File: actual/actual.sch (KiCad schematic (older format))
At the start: 32 parts

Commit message: Monday night hacking
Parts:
- removed C?: C, symbol Device:C
- removed P?: Conn_WallPlug_Earth, symbol Connector:Conn_WallPlug_Earth
- removed SW?: GROUND, symbol Switch:SW_SPDT
- added J?: IEC_SOCKET, symbol yga1:IEC_SOCKET
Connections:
- wire segments 80 -> 76
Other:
- moved on the sheet: F?, SW?
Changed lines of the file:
@@
 L Device:Fuse F?
 U 1 1 5C5654FC
-P 1600 5550
-F 0 "F?" V 1403 5550 50  0000 C CNN
-F 1 "Fuse" V 1494 5550 50  0000 C CNN
-F 2 "" V 1530 5550 50  0001 C CNN
-F 3 "~" H 1600 5550 50  0001 C CNN
-	1    1600 5550
+P 2150 5150
+F 0 "F?" V 1953 5150 50  0000 C CNN
+F 1 "Fuse" V 2044 5150 50  0000 C CNN
+F 2 "" V 2080 5150 50  0001 C CNN
+F 3 "~" H 2150 5150 50  0001 C CNN
+	1    2150 5150
 	0    1    1    0
 $EndComp
 $Comp
-L Connector:Conn_WallPlug_Earth P?
-U 1 1 5C5655DC
-P 1000 5350
-F 0 "P?" H 1065 5675 50  0000 C CNN
-F 1 "Conn_WallPlug_Earth" H 1065 5584 50  0000 C CNN
-F 2 "" H 1400 5350 50  0001 C CNN
-F 3 "~" H 1400 5350 50  0001 C CNN
-	1    1000 5350
-	1    0    0    -1
-$EndComp
-$Comp
 L power:Earth #PWR?
 U 1 1 5C56566E
-P 1300 5800
-F 0 "#PWR?" H 1300 5550 50  0001 C CNN
-F 1 "Earth" H 1300 5650 50  0001 C CNN
-F 2 "" H 1300 5800 50  0001 C CNN
-F 3 "~" H 1300 5800 50  0001 C CNN
-	1    1300 5800
-	1    0    0    -1
-$EndComp
-Wire Wire Line
-	1300 5650 1300 5800
-Wire Wire Line
-	1300 5450 1300 5550
-Wire Wire Line
-	1300 5550 1450 5550
-Wire Wire Line
-	2450 5550 1850 5550
-$Comp
-L Switch:SW_SPST SW?
-U 1 1 5C5657AA
-P 1500 5150
-F 0 "SW?" H 1500 5385 50  0000 C CNN
-F 1 "A.C." H 1500 5294 50  0000 C CNN
-F 2 "" H 1500 5150 50  0001 C CNN
-F 3 "" H 1500 5150 50  0001 C CNN
-	1    1500 5150
-	1    0    0    -1
-$EndComp
-Wire Wire Line
-	1300 5250 1300 5150
-Wire Wire Line
-	1700 5150 1850 5150
-$Comp
-L Switch:SW_SPDT SW?
-U 1 1 5C5658F5
-P 2050 5350
-F 0 "SW?" H 2050 5635 50  0000 C CNN
-F 1 "GROUND" H 2050 5544 50  0000 C CNN
-F 2 "" H 2050 5350 50  0001 C CNN
-F 3 "" H 2050 5350 50  0001 C CNN
-	1    2050 5350
-	-1   0    0    -1
-$EndComp
-Wire Wire Line
-	1850 5250 1850 5150
-Connection ~ 1850 5150
-Wire Wire Line
-	1850 5450 1850 5550
-Connection ~ 1850 5550
-Wire Wire Line
-	1850 5550 1750 5550
-$Comp
-L Device:C C?
-U 1 1 5C565A52
-P 2250 5750
-F 0 "C?" H 2365 5796 50  0000 L CNN
-F 1 "C" H 2365 5705 50  0000 L CNN
-F 2 "" H 2288 5600 50  0001 C CNN
-F 3 "~" H 2250 5750 50  0001 C CNN
-	1    2250 5750
-	1    0    0    -1
-$EndComp
-$Comp
-L power:Earth #PWR?
-U 1 1 5C565AE5
-P 2250 5950
-F 0 "#PWR?" H 2250 5700 50  0001 C CNN
-F 1 "Earth" H 2250 5800 50  0001 C CNN
-F 2 "" H 2250 5950 50  0001 C CNN
-F 3 "~" H 2250 5950 50  0001 C CNN
-	1    2250 5950
-	1    0    0    -1
-$EndComp
-Wire Wire Line
-	2250 5350 2250 5600
-Wire Wire Line
-	2250 5900 2250 5950
-Wire Wire Line
-	1850 5150 2450 5150
+P 1500 5800
+F 0 "#PWR?" H 1500 5550 50  0001 C CNN
+F 1 "Earth" H 1500 5650 50  0001 C CNN
+F 2 "" H 1500 5800 50  0001 C CNN
+F 3 "~" H 1500 5800 50  0001 C CNN
+	1    1500 5800
+	1    0    0    -1
+$EndComp
+Wire Wire Line
+	1400 5450 1400 5550
 $Comp
 L Device:Lamp LA?
@@
 Wire Wire Line
 	2550 2400 2550 2850
+Wire Wire Line
+	1400 5550 2450 5550
+Wire Wire Line
+	2000 5150 1950 5150
+Wire Wire Line
+	2300 5150 2450 5150
+$Comp
+L yga1:IEC_SOCKET J?
+U 1 1 5C64456C
+P 1400 5350
+F 0 "J?" H 950 5650 50  0000 C CNN
+F 1 "IEC_SOCKET" H 1100 5550 50  0000 C CNN
+F 2 "" H 1300 5350 50  0001 C CNN
+F 3 "" H 1300 5350 50  0001 C CNN
+	1    1400 5350
+	1    0    0    -1
+$EndComp
+Wire Wire Line
+	1400 5250 1400 5150
+$Comp
+L Switch:SW_SPST SW?
+U 1 1 5C5657AA
+P 1750 5150
+F 0 "SW?" H 1750 5385 50  0000 C CNN
+F 1 "A.C." H 1750 5294 50  0000 C CNN
+F 2 "" H 1750 5150 50  0001 C CNN
+F 3 "" H 1750 5150 50  0001 C CNN
+	1    1750 5150
+	1    0    0    -1
+$EndComp
+Wire Wire Line
+	1400 5150 1550 5150
+Wire Wire Line
+	1500 5350 1400 5350
+Wire Wire Line
+	1500 5350 1500 5800
 $EndSCHEMATC

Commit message: Update schematic and design reverb unit
Create a schematic to capture all the changes that have been done. There have been many small fiddle things but not even an electronic version of the full schematic.
Find a schematic for a reverb unit and add it to the amp schematic.
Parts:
- removed J?: CH2, symbol Connector:Conn_01x01_Male
- removed J?: CH1, symbol Connector:Conn_01x01_Male
- removed J?: CH1 volume pot (4M), symbol Connector:Conn_01x03_Male
- removed J?: Earth, symbol Connector:Conn_01x01_Male
- removed J?: CH2 volume pot (4M), symbol Connector:Conn_01x03_Male
- removed J?: Audio Out, symbol Connector:Conn_01x01_Male
- removed V? (x2): 12AX7A, symbol yga1:12AX7A
- added C1: 270uF 16V, symbol Device:CP
- added C10, C11, C15, C6: 0.1uF 400V, symbol Device:C
- added C12, C13: 8.2uF 250V, Capacitor_THT:CP_Radial_D8.0mm_P5.00mm, symbol Device:CP
- added C14: 0.047uF 600V, symbol Device:C
- added C16: 25uF 25V, symbol Device:C
- added C17: 0.02uF, 0.02uF, symbol Device:C
- added C18, C19: 0.01uF, symbol Device:C
- added C2, C4: 0.02uF 400V, symbol Device:C
- added C20: 47n, symbol Device:C
- added C27: 10uF 400V, symbol Device:C
- added C28: 1uF 16V, symbol Device:CP
- added C29, C33: 22uF 50V, symbol Device:CP
- added C3: 40uF, symbol Device:C
- added C30: 0.01uF 400V, symbol Device:C
- added C31: 100n, symbol Device:C
- added C32: 2n2, symbol Device:C
- added C34: 1uF, symbol Device:CP
- added C35: 220uF, symbol Device:CP
- added C36: 100nF 400V, symbol Device:C
- added C37: 10n, symbol Device:C
- added C38: 250pF, symbol Device:C
- added C5: 270pF, symbol Device:C
- added C7: 0.02uF, symbol Device:C
- added C8: 0.02 400V, symbol Device:C
- added C9: 0.1uF, symbol Device:C
- added D1: PH204, Diode_SMD:D_SMA, symbol Device:D
- added J1: in_lo, symbol yga1:AudioJack2_Switch
- added J10: effect return, symbol yga1:AudioJack2_Switch
- added J2: in_hi, symbol yga1:AudioJack2_Switch
- added J4: Tank IN, symbol Connector:Conn_Coaxial
- added J5: Audio Out, symbol Connector:AudioJack2
- added J6: Reverb Footswitch, symbol Connector:AudioJack2
- added J7: tremolo footswitch, symbol yga1:jack_0.25in_mono
- added J8: Tank OUT, symbol Connector:Conn_Coaxial
- added J9: effect send, symbol yga1:AudioJack2_Switch
- added R1, R19, R2: 68K, symbol Device:R
- added R10, R3, R37, R39, R56, R59: 1M, symbol Device:R
- added R11, R13, R15, R16, R25, R28, R40, R46, R49, R57: 100K, symbol Device:R
- added R12, R7: 820, symbol Device:R
- added R14: 10K 1W, symbol Device:R
- added R17: 27K, symbol Device:R
- added R18, R26, R27, R34, R51: 220K, symbol Device:R
- added R20, R22, R35, R36, R61: 470K, symbol Device:R
- added R21: 470, symbol Device:R
- added R23, R38: 4.7K, symbol Device:R
- added R24: 82K, symbol Device:R
- added R29, R30: 470 1W, symbol Device:R
- added R31: 150K, Resistor_THT:R_Axial_DIN0309_L9.0mm_D3.2mm_P12.70mm_Horizontal, symbol Device:R
- added R32: 15K, Resistor_THT:R_Axial_DIN0207_L6.3mm_D2.5mm_P10.16mm_Horizontal, symbol Device:R
- added R33: 56K, Resistor_THT:R_Axial_DIN0207_L6.3mm_D2.5mm_P10.16mm_Horizontal, symbol Device:R
- added R4: 4.7K 1W, symbol Device:R
- added R44: 10K 1/2W, symbol Device:R
- added R45: 1K, symbol Device:R
- added R47: 2.7K, symbol Device:R
- added R48: 100k, symbol Device:R
- added R5, R6: 2M2, symbol Device:R
- added R50: 1.5K, symbol Device:R
- added R52: 33K, symbol Device:R
- added R53: 2K2, symbol Device:R
- added R54: 4k7, symbol Device:R
- added R55: 1K 2W, symbol Device:R
- added R58: 1K5 1/2 watt, symbol Device:R
- added R8, R9: 100K 1/2W, symbol Device:R
- added RV1, RV2: 1M, symbol Device:R_POT
- added RV10: 100, symbol Device:R_POT
- added RV3: Treble Pot (250K), symbol Device:R_POT
- added RV4: Bass Pot (1M), symbol Device:R_POT
- added RV5: Intensity pot (1M), symbol Device:R_POT
- added RV6: Speed pot (250K), symbol Device:R_POT
- added RV7: 250kA, symbol Device:R_POT
- added RV8: 250kB, symbol Device:R_POT
- added RV9: 50kB, symbol Device:R_POT
- added S1: regular/crunch, symbol local:SW_SPDT
- added T2: 68348, symbol Device:Transformer_SP_1S
- added T3: Transformer_125ASE, symbol yga1:Transformer_125ASE
- added V1, V2, V3, V6, V8: 12AX7, Valve:Valve_ECC-83-1, symbol local:12AX7
- added V4, V5: 7027A, symbol yga1:7027A
- added V7: 12AT7, Valve:Valve_ECC-83-1, symbol local:12AT7
- added V9: EL84, symbol local:EL84
- R42: renamed from R?; value R -> 100K, 2W
- R43: renamed from R?; value 4.7K -> 4.7K 1W
- gave numbers to parts that had none: 20
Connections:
- net B+: now also R13.1, R14.2, R24.2, R25.1, R36.2, V2.1 (a), V6.6 (a)
- net Earth: now also C1.2, C12.1, C13.1, C14.2, C16.2, C27.2, C28.2, C29.2, C3.2, C33.2, C34.2, C35.2, C37.2, J1.S, J10.S, J2.S, J2.TN, J4.2 (Ext), J5.S, J6.S, J7.2, J8.2 (Ext), J9.S, R10.2, R12.2, R15.2, R17.2, R18.2, R23.2, R3.2, R33.2, R35.2, R38.2, R39.2, R40.2, R45.2, R46.2, R47.2, R50.2, R52.2, R55.2, R56.2, R58.2, R59.2, R6.2, R7.2, RV1.1, RV2.1, RV8.3, T2.4 (S1), T3.BLK (0h), V4.8 (C), V5.8 (C)
- net f1: now also V1.4 (f), V1.5 (f), V2.4 (f), V2.5 (f), V3.5 (f), V3.9 (f), V4.2, V5.7, V6.9 (f), V6.9 (f), V7.4 (f), V7.5 (f), V8.4 (f), V8.5 (f), V9.5 (f)
- net f2: now also V1.9 (f), V1.9 (f), V2.9 (f), V2.9 (f), V3.4 (f), V3.9 (f), V4.7, V5.2, V6.4 (f), V6.5 (f), V7.9 (f), V7.9 (f), V8.9 (f), V8.9 (f), V9.4 (f)
- net at D2.2 (A), T1.6: now also R31.2
- net V1: now reaches L1.1, SW3.2 (B)
- net V1: now also T2.2 (PM)
- net V2: now reaches C25.1, L1.2, R43.2
- net V2: now also R4.2, RV10.2
- new net: C28.1, R47.1, V1.3 (k)
- new net: C2.2, R8.1, V1.1 (a)
- new net: C27.1, R14.1, R8.2, R9.2
- new net: C2.1, RV1.3
- new net: C4.2, R9.1, V1.6 (a)
- new net: C4.1, RV2.3
- new net: R11.1, RV2.2
- new net: R11.2, V2.7 (g)
- new net: J1.TN, J2.T, R2.2
- new net: R1.1, R2.1, R3.1, S1.2, V1.2 (g)
- new net: J1.T, R1.2
- new net: R59.1, S1.1, V1.7 (g)
- new net: RV1.2, S1.3
- new net: C1.1, R7.1, V1.8 (k)
- new net: R13.2, V2.2 (g), V2.6 (a)
- new net: C34.1, R12.1, V2.8 (k)
- new net: C5.2, R15.1, R16.1, V2.3 (k)
- new net: C6.1, R16.2
- new net: C6.2, RV4.1
- new net: C5.1, RV3.1
- new net: C7.2, R17.1, RV4.3
- new net: C7.1, R18.1, RV3.3, RV4.2
- new net: J9.T, RV3.2
- new net: R53.1, V9.2 (g1)
- new net: C33.1, R55.1, V9.3 (k)
- new net: T3.BLU (IN-), V9.7 (a)
- new net: R54.2, V9.9 (g2)
- new net: C3.1, R4.1, R44.1, R49.1, R5.1, R54.1, R57.1, T3.BRN (IN+), V8.6 (a)
- new net: C20.1, R5.2, R6.1, V8.7 (g)
- new net: C31.2, R46.1, V8.8 (k)
- new net: C11.2, R25.2, V3.1 (a)
- new net: C9.1, R22.2, V3.2 (g)
- new net: R21.1, V3.3 (k), V3.8 (k)
- new net: R48.2, V7.6 (a)
- new net: C20.2, J10.T, R10.1, V7.7 (g)
- new net: C29.1, R45.1, V7.8 (k)
- new net: C32.2, R49.2, V7.1 (a)
- new net: RV8.2, V7.2 (g)
- new net: R50.1, V7.3 (k)
- new net: J10.TN, J9.TN
- new net: T2.1 (PR1), V4.3 (A)
- new net: R29.1, V4.4
- new net: C10.1, R27.1, V4.5 (G)
- new net: T2.3 (PR2), V5.3 (A)
- new net: R30.2, V5.4
- new net: C11.1, R26.2, V5.5 (G)
- new net: C8.1, R20.1, V3.7 (g)
- new net: C8.2, RV7.2
- new net: C9.2, R19.2, R23.1, R28.1
- new net: R19.1, R20.2, R21.2, R22.1
- new net: C10.2, R24.1, V3.6 (a)
- new net: C14.1, R26.1, R27.2, RV5.2
- new net: J5.T, R28.2, T2.5 (S2)
- new net: R29.2, RV10.1
- new net: R30.1, RV10.3
- new net: C15.1, R34.2
- new net: C15.2, RV5.1
- new net: R34.1, R35.1, V6.8 (k)
- new net: C17.2, R36.1, V6.1 (a), V6.7 (g)
- new net: C18.2, C19.1, J7.1, R37.1
- new net: C16.1, R37.2, R38.1, V6.3 (k)
- new net: C17.1, C18.1, RV6.1
- new net: C19.2, R39.1
- new net: R40.1, RV6.2
- new net: D1.1 (K), R31.1
- new net: C12.2, D1.2 (A), R32.2
- new net: C36.2, R57.2, V8.1 (a)
- new net: J6.T, J8.1 (In), R56.1, V8.2 (g)
- new net: C35.1, R58.1, V8.3 (k)
- new net: C30.2, R44.2, R48.1
- new net: C30.1, R61.2
- new net: R61.1, RV8.1
- new net: C32.1, R51.1
- new net: R51.2, R52.1, R53.2
- new net: J4.1 (In), T3.YEL (8h)
- new net: C31.1, RV7.3
- new net: C36.1, RV9.1
- new net: C37.1, RV9.3
- new net: C38.2, RV9.2
- new net: C38.1, RV7.1
- new net -40V: C13.2, R32.1, R33.1, RV5.3
- no-connect marks 0 -> 1
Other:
- moved on the sheet: C21, C22, C23, C24, C25, C26, D2, D3, D4, D5, D6, D7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

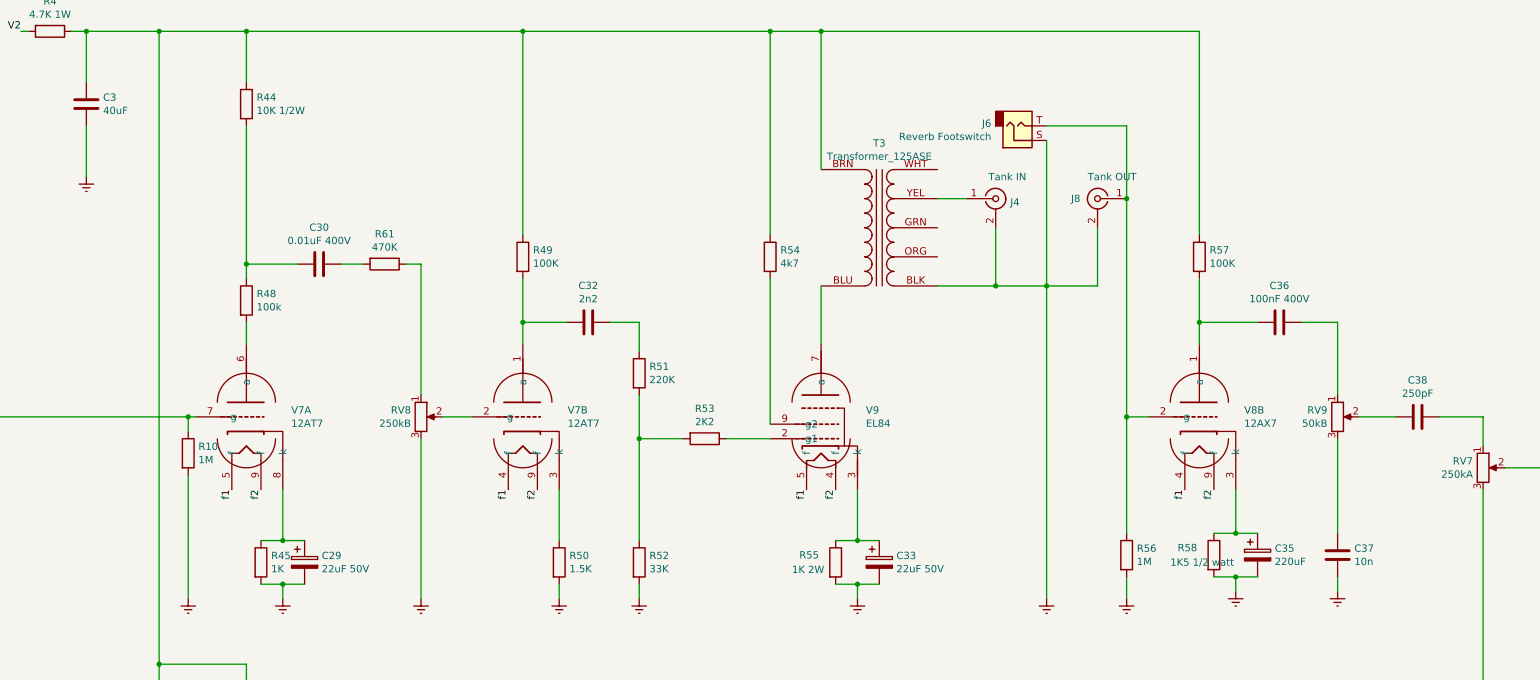
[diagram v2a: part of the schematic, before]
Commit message: parts list and order for reverb driver circuit
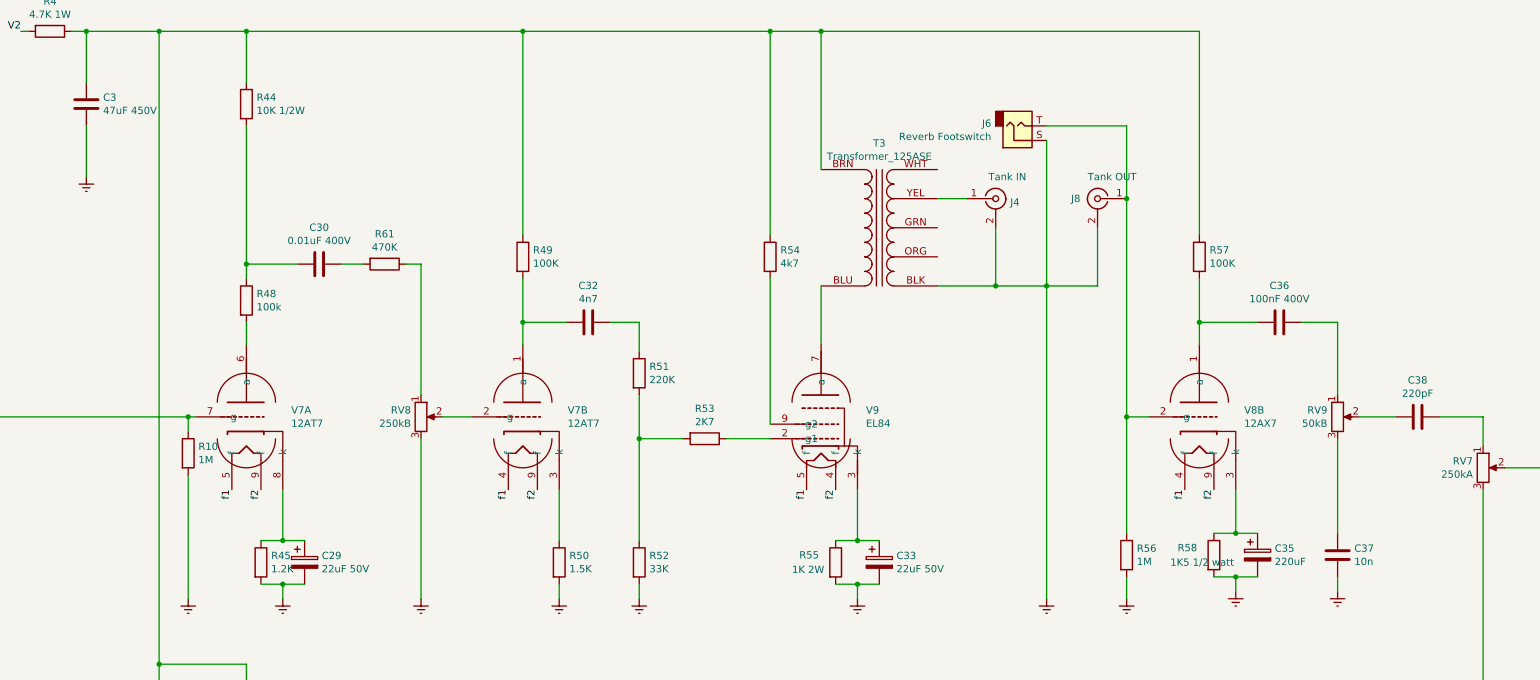
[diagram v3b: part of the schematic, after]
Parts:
- C3: value 40uF -> 47uF 450V
- C32: value 2n2 -> 4n7
- C38: value 250pF -> 220pF
- R45: value 1K -> 1.2K
- R53: value 2K2 -> 2K7
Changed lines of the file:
@@
 P 3350 9550
 F 0 "R45" H 3420 9596 50  0000 L CNN
-F 1 "1K" H 3420 9505 50  0000 L CNN
+F 1 "1.2K" H 3420 9505 50  0000 L CNN
 F 2 "" V 3280 9550 50  0001 C CNN
 F 3 "~" H 3350 9550 50  0001 C CNN
@@
 P 5600 7900
 F 0 "C32" V 5348 7900 50  0000 C CNN
-F 1 "2n2" V 5439 7900 50  0000 C CNN
+F 1 "4n7" V 5439 7900 50  0000 C CNN
 F 2 "" H 5638 7750 50  0001 C CNN
 F 3 "~" H 5600 7900 50  0001 C CNN
@@
 P 6400 8700
 F 0 "R53" V 6193 8700 50  0000 C CNN
-F 1 "2K2" V 6284 8700 50  0000 C CNN
+F 1 "2K7" V 6284 8700 50  0000 C CNN
 F 2 "" V 6330 8700 50  0001 C CNN
 F 3 "~" H 6400 8700 50  0001 C CNN
@@
 P 11300 8550
 F 0 "C38" V 11048 8550 50  0000 C CNN
-F 1 "250pF" V 11139 8550 50  0000 C CNN
+F 1 "220pF" V 11139 8550 50  0000 C CNN
 F 2 "" H 11338 8400 50  0001 C CNN
 F 3 "~" H 11300 8550 50  0001 C CNN
@@
 P 2150 6400
 F 0 "C3" H 2265 6446 50  0000 L CNN
-F 1 "40uF" H 2265 6355 50  0000 L CNN
+F 1 "47uF 450V" H 2265 6355 50  0000 L CNN
 F 2 "" H 2188 6250 50  0001 C CNN
 F 3 "~" H 2150 6400 50  0001 C CNN

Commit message: more tinkering
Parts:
- added C39, C40, C41: 0.001uF 630V, symbol Device:C
- added R60: 1K, symbol Device:R
- added R62, R63: 360K, symbol Device:R
- C18, C19: value 0.01uF -> 0.02uF
- C8: value 0.02 400V -> 0.047 400V
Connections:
- net B+: now also C41.1
- net at C2.2, R8.1, V1.1 (a): now also C39.2
- net at C27.1, R14.1, R8.2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: now also C39.1, C40.1
- net at C2.1: now also R62.1; no longer RV1.3
- net at C4.2, R9.1, V1.6 (a): now also C40.2
- net at C4.1: now also R63.1; no longer RV2.3
- net at R59.1, V1.7 (g): now also R60.1; no longer S1.1
- net at R13.2, V2.2 (g), V2.6 (a): now also C41.2
- new net: R60.2, S1.1
- new net: R62.2, RV1.3
- new net: R63.2, RV2.3
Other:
- moved on the sheet: C2, C4, R11, R13, RV1, RV2, V2B

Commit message: update schematic after assembling reverb unit
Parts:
- added J11: PWR, symbol Connector:Screw_Terminal_01x02
- added J12: el84, symbol Connector:Screw_Terminal_01x02
- added J13: V_power, symbol Connector:Screw_Terminal_01x04
- added J14: RG, symbol Connector:Screw_Terminal_01x04
- added J15: RC, symbol Connector:Screw_Terminal_01x04
- added J16, J17, J18: 105-1103-001, digikey-footprints:Test_Jack_Horiz, symbol dk_Banana-and-Tip-Connectors-Jacks-Plugs:105-1103-001
- added R64: 220K, symbol Device:R
- added TP1, TP10, TP11, TP12, TP13, TP14, TP15, TP16, TP17, TP18, TP19, TP2, TP20, TP21, TP22, TP23, TP24, TP25, TP26, TP27, TP28, TP29, TP3, TP30, TP31, TP32, TP33, TP34, TP4, TP5, TP6, TP7, TP8, TP9: TestPoint, symbol Connector:TestPoint
- C20: value 47n -> 47nF
- C29, C33: value 22uF 50V -> 27uF 25V
- C31: value 100n -> 0.1uF
- C32: value 4n7 -> 4.7nF
- C36: value 100nF 400V -> 0.1uF 400V
- C38: value 220pF -> 330pF
- R53: value 2K7 -> 2.7K
- R54: value 4k7 -> 4.7K
- R8: value 100K 1/2W -> 220K 1/2W
- RV7: Function (none) -> Mix
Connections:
- net -40V: now also TP13.1
- net B+: now also TP16.1, TP19.1
- net Earth: now also RV8.1, J11.1 (Pin_1), R64.2; no longer RV8.3
- net V2: now also R54.1, T3.BRN (IN+), J11.2 (Pin_2), J12.2 (Pin_2), J16.1, TP31.1
- net at C28.1, R47.1, V1.3 (k): now also TP5.1
- net at C27.1, C39.1, C40.1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: now also TP2.1
- net at C2.1, R62.1: now also TP8.1
- net at C4.1, R63.1: now also TP14.1
- net at C1.1, R7.1, V1.8 (k): now also TP10.1
- net at C34.1, R12.1, V2.8 (k): now also TP17.1
- net at C5.2, R15.1, R16.1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: now also TP20.1
- net at J9.T, RV3.2: now also TP24.1
- net rg1: now reaches R53.1, V9.2 (g1)
- net rc3: now reaches C33.1, R55.1, V9.3 (k)
- net rc3: now also J15.3 (Pin_3), TP15.1
- net el84_1: now reaches R54.2, V9.9 (g2)
- net el84_1: now also J12.1 (Pin_1)
- net rp4: now reaches C3.1, R4.1, R44.1, R49.1, R5.1, R57.1, V8.6 (a)
- net rp4: now also R64.1, TP1.1; no longer R54.1, T3.BRN (IN+)
- net rg3: now reaches C20.1, R5.2, R6.1, V8.7 (g)
- net rg3: now also J14.3 (Pin_3), TP3.1
- net at R46.1, V8.8 (k): now also C31.1, TP7.1; no longer C31.2
- net at C9.1, R22.2, V3.2 (g): now also TP27.1
- net at R21.1, V3.3 (k), V3.8 (k): now also TP28.1
- net rvp3: now reaches R48.2, V7.6 (a)
- net rvp3: now also J13.3 (Pin_3)
- net rc1: now reaches C20.2, J10.T, R10.1, V7.7 (g)
- net rc1: now also J14.4 (Pin_4), J15.1 (Pin_1)
- net rc4: now reaches C29.1, R45.1, V7.8 (k)
- net rc4: now also J15.4 (Pin_4), TP4.1
- net rp2: now reaches C32.2, R49.2, V7.1 (a)
- net at R50.1, V7.3 (k): now also TP9.1
- net at R29.1, V4.4: now also J17.1, TP32.1
- net at C10.1, R27.1, V4.5 (G): now also TP29.1
- net at R30.2, V5.4: now also J18.1, TP33.1
- net at C11.1, R26.2, V5.5 (G): now also TP30.1
- net at C8.1, R20.1, V3.7 (g): now also TP26.1
- net at C8.2, RV7.2: now also TP25.1
- net at J5.T, R28.2, T2.5 (S2): now also TP34.1
- net at C19.2, R39.1: now also V6.2 (g)
- net rvp1: now reaches C36.2, R57.2, V8.1 (a)
- net rvp1: now also J13.1 (Pin_1)
- net at J6.T, J8.1 (In), R56.1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: now also TP21.1
- net rc2: now reaches C35.1, R58.1, V8.3 (k)
- net rc2: now also J15.2 (Pin_2), TP22.1
- net at C30.1, R61.2: now also TP6.1
- net rg2: now reaches R61.1
- net rg2: now also RV8.3; no longer RV8.1
- net at C32.1, R51.1: now also TP11.1
- net at R51.2, R52.1, R53.2: now also TP12.1
- net at J4.1 (In), T3.YEL (8h): now also TP18.1
- net at RV7.3: now also C38.1; no longer C31.1
- net at C36.1, RV9.1: now also TP23.1
- net at RV7.1: now also C31.2; no longer C38.1
- new net rvp2: J13.2 (Pin_2)
- new net rvp4: J13.4 (Pin_4)
- new net vg1: J14.1 (Pin_1)
- new net vg2: J14.2 (Pin_2)
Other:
- moved on the sheet: C20, C3, C30, C31, C36, C5, R4, R46, R54, R61, V8A

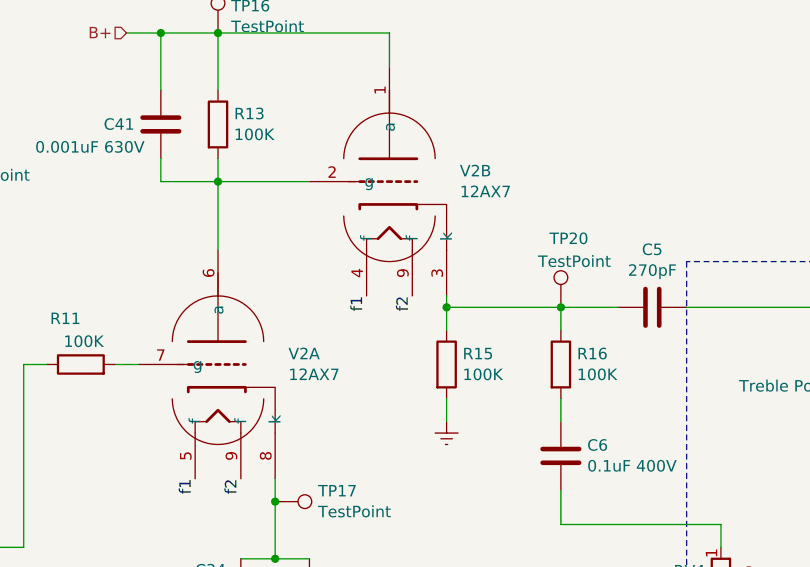
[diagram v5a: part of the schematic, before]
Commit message: swap V2 for 12AT7
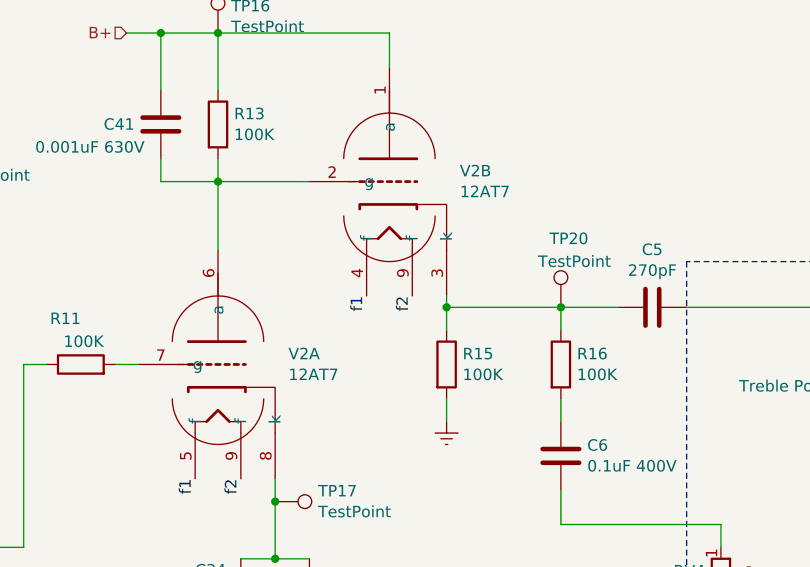
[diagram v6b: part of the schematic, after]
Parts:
- V2: value 12AX7 -> 12AT7
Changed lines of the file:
@@
 P 7650 2700
 F 0 "V2" H 7958 2696 50  0000 L CNN
-F 1 "12AX7" H 7958 2605 50  0000 L CNN
+F 1 "12AT7" H 7958 2605 50  0000 L CNN
 F 2 "Valve:Valve_ECC-83-1" H 7670 2700 50  0001 C CNN
 F 3 "" H 7670 2700 50  0001 C CNN
@@
 P 8400 1900
 F 0 "V2" H 8708 1896 50  0000 L CNN
-F 1 "12AX7" H 8708 1805 50  0000 L CNN
+F 1 "12AT7" H 8708 1805 50  0000 L CNN
 F 2 "Valve:Valve_ECC-83-1" H 8420 1900 50  0001 C CNN
 F 3 "" H 8420 1900 50  0001 C CNN
